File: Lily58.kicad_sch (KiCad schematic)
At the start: 40 parts, among them J1 USB_C_Receptacle, J2 USB_C_Receptacle, J3 Conn_01x03_Pin, U1 BQ24091DGQ, U2 TPS63000, U3 TPS63000, U4 ESP32-S3-WROOM-1, Y1 Crystal_GND24

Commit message: restructured schematic
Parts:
- removed U4: ESP32-S3-WROOM-1, PCM_Espressif:ESP32-S3-WROOM-1, symbol PCM_Espressif:ESP32-S3-WROOM-1
- removed Y1: Crystal_GND24, Crystal:Crystal_SMD_3225-4Pin_3.2x2.5mm_HandSoldering, symbol Device:Crystal_GND24
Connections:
- net +5V: no longer C11.1, J1.A4 (VBUS), J1.A9 (VBUS), J1.B4 (VBUS), J1.B9 (VBUS), J2.A4 (VBUS), J2.A9 (VBUS), J2.B4 (VBUS), J2.B9 (VBUS), U1.1 (IN)
- new net USB_5V: C11.1, J1.A4 (VBUS), J1.A9 (VBUS), J1.B4 (VBUS), J1.B9 (VBUS), J2.A4 (VBUS), J2.A9 (VBUS), J2.B4 (VBUS), J2.B9 (VBUS), U1.1 (IN)
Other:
- added sheet Microcontroller (microcontroller.kicad_sch)
- moved on the sheet: C1, C10, C11, C12, C2, C3, C4, C5, C6, C7, C8, C9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

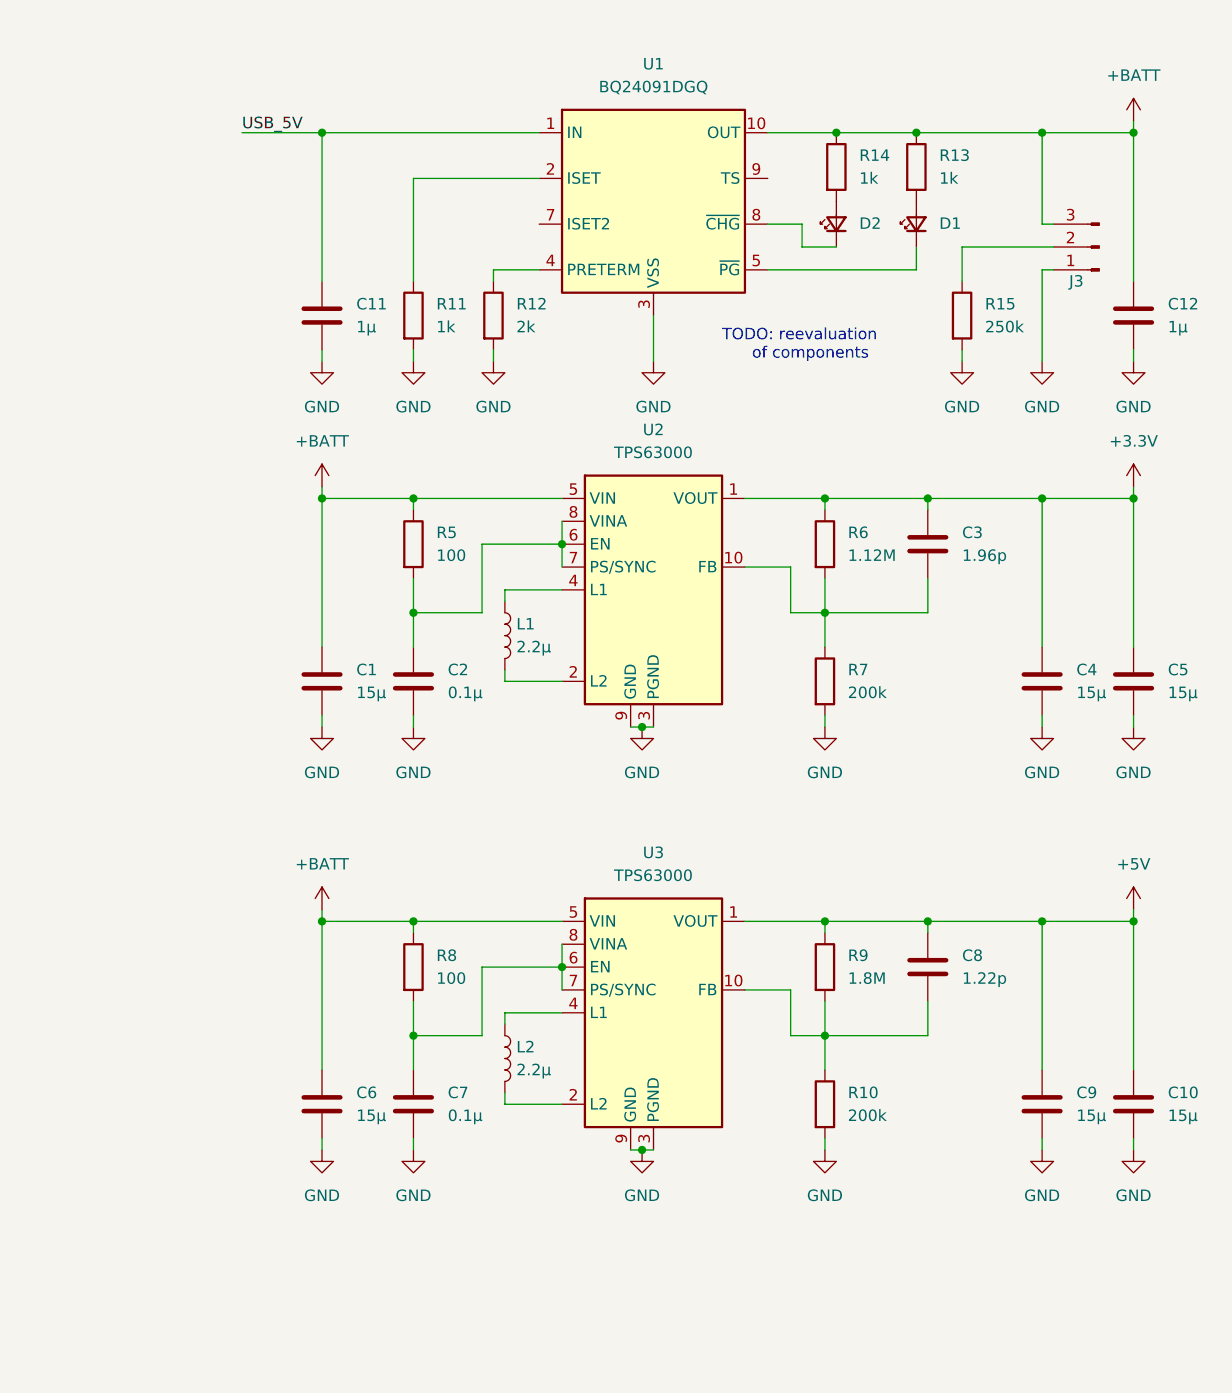
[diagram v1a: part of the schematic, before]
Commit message: configured battery charger circuit
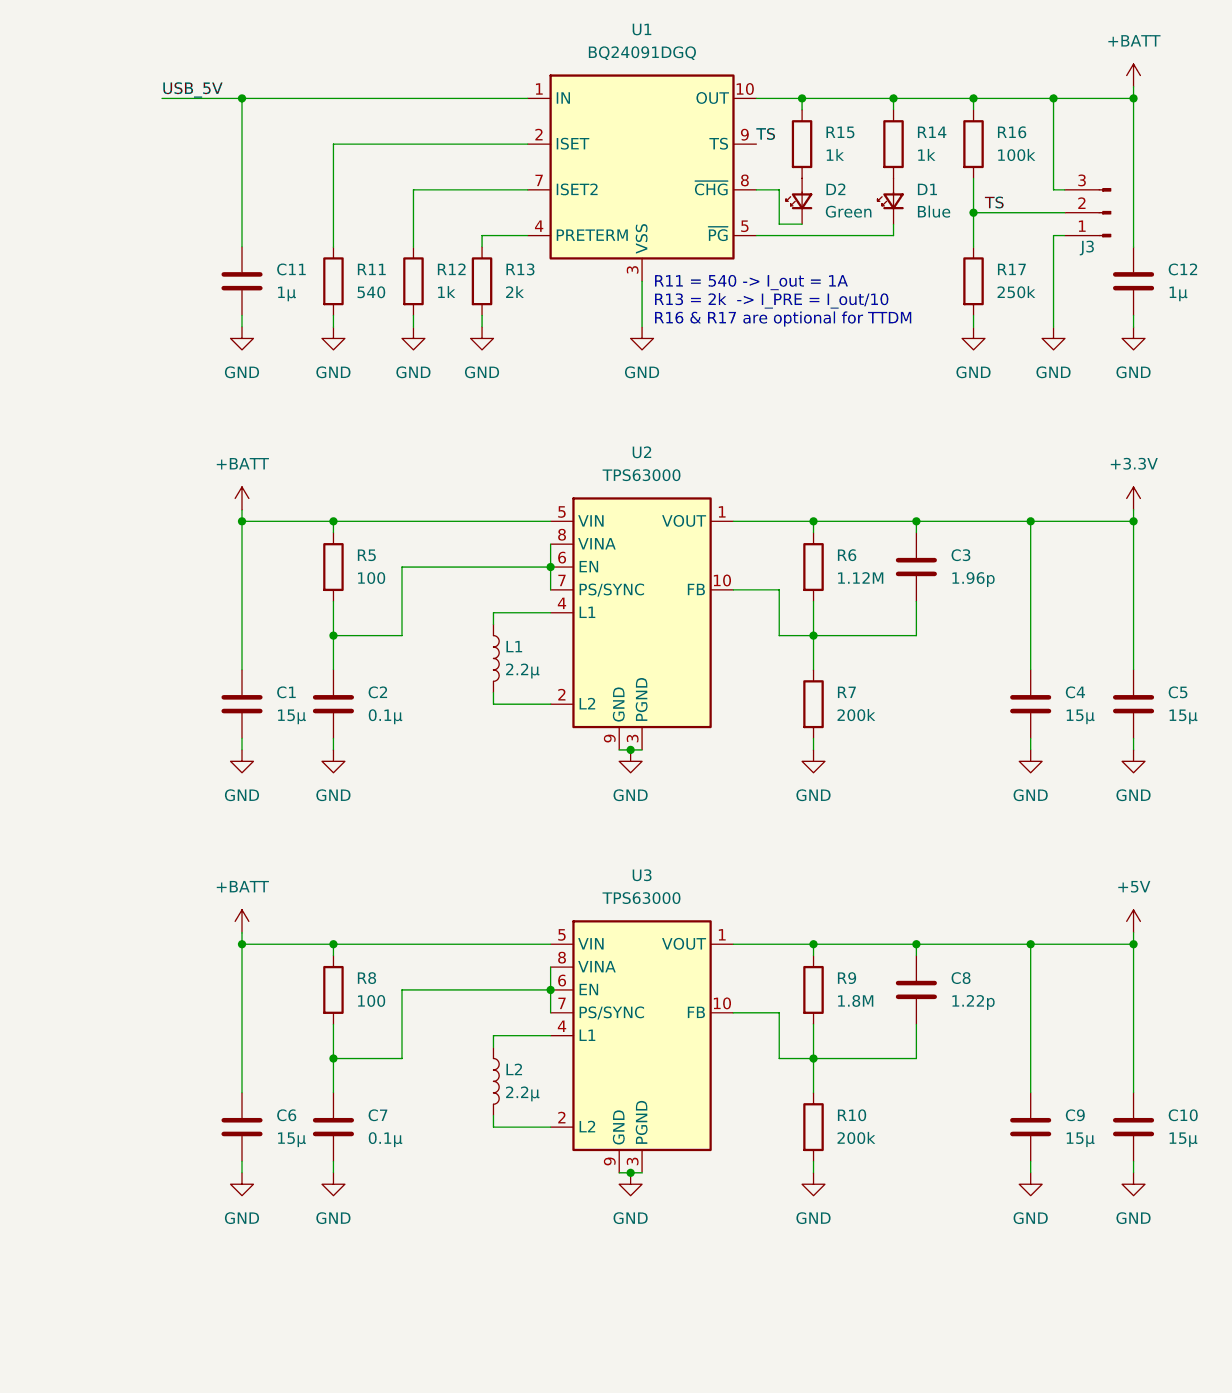
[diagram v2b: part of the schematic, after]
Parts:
- added R12: 1k, symbol Device:R
- added R16: 100k, symbol Device:R
- D1: value LED_Small -> Blue
- D2: value LED_Small -> Green
- R11: value 1k -> 540
- renumbered R12 to R13, R13 to R14, R14 to R15, R15 to R17
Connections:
- net +BATT: now also R16.1
- net GND: now also R12.2
- net TS: now reaches J3.2 (Pin_2), R17.1
- net TS: now also U1.9 (TS), R16.2
- net at U1.7 (ISET2): now also R12.1
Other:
- note added: "R11 = 540 -> I_out = 1A R13 = 2k -> I_PRE = I_out/10 R16 & R17 are optional for TTDM"
- note removed: "TODO: reevaluation of components"
- moved on the sheet: C1, C10, C11, C12, C2, C3, C4, C5, C6, C7, C8, C9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

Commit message: reworked component naming
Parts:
- renumbered C1 to C21, C2 to C22, C3 to C23, C4 to C24, C5 to C25, C6 to C31, C7 to C32, C8 to C33, C9 to C34, C10 to C35, L1 to L21, L2 to L31, R5 to R21, R6 to R22, R7 to R23, R8 to R31, R9 to R32, R10 to R33
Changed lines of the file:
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@@
   (symbol (lib_id "Device:C") (at 182.88 97.79 0) (unit 1)
     (in_bom yes) (on_board yes) (dnp no) (fields_autoplaced)
-    (property "Reference" "C2" (at 186.69 96.52 0)
+    (property "Reference" "C22" (at 186.69 96.52 0)
       (effects (font (size 1.27 1.27)) (justify left))
     )
@@
       (project "Lily58"
         (path "/a0958e12-2248-4ac3-b259-3086ac296b70"
-          (reference "C2") (unit 1)
+          (reference "C22") (unit 1)
         )
       )
@@
   (symbol (lib_id "Device:C") (at 271.78 97.79 0) (unit 1)
     (in_bom yes) (on_board yes) (dnp no) (fields_autoplaced)
-    (property "Reference" "C5" (at 275.59 96.52 0)
+    (property "Reference" "C25" (at 275.59 96.52 0)
       (effects (font (size 1.27 1.27)) (justify left))
     )
@@
       (project "Lily58"
         (path "/a0958e12-2248-4ac3-b259-3086ac296b70"
-          (reference "C5") (unit 1)
+          (reference "C25") (unit 1)
         )
       )
@@
   (symbol (lib_id "Device:L") (at 200.66 139.7 0) (unit 1)
     (in_bom yes) (on_board yes) (dnp no) (fields_autoplaced)
-    (property "Reference" "L2" (at 201.93 138.43 0)
+    (property "Reference" "L31" (at 201.93 138.43 0)
       (effects (font (size 1.27 1.27)) (justify left))
     )
@@
       (project "Lily58"
         (path "/a0958e12-2248-4ac3-b259-3086ac296b70"
-          (reference "L2") (unit 1)
+          (reference "L31") (unit 1)
         )
       )
@@
   (symbol (lib_id "Device:C") (at 247.65 129.54 0) (unit 1)
     (in_bom yes) (on_board yes) (dnp no) (fields_autoplaced)
-    (property "Reference" "C8" (at 251.46 128.27 0)
+    (property "Reference" "C33" (at 251.46 128.27 0)
       (effects (font (size 1.27 1.27)) (justify left))
     )
@@
       (project "Lily58"
         (path "/a0958e12-2248-4ac3-b259-3086ac296b70"
-          (reference "C8") (unit 1)
+          (reference "C33") (unit 1)
         )
       )
@@
   (symbol (lib_id "Device:C") (at 271.78 144.78 0) (unit 1)
     (in_bom yes) (on_board yes) (dnp no) (fields_autoplaced)
-    (property "Reference" "C10" (at 275.59 143.51 0)
+    (property "Reference" "C35" (at 275.59 143.51 0)
       (effects (font (size 1.27 1.27)) (justify left))
     )
@@
       (project "Lily58"
         (path "/a0958e12-2248-4ac3-b259-3086ac296b70"
-          (reference "C10") (unit 1)
+          (reference "C35") (unit 1)
         )
       )
@@
   (symbol (lib_id "Device:L") (at 200.66 92.71 0) (unit 1)
     (in_bom yes) (on_board yes) (dnp no) (fields_autoplaced)
-    (property "Reference" "L1" (at 201.93 91.44 0)
+    (property "Reference" "L21" (at 201.93 91.44 0)
       (effects (font (size 1.27 1.27)) (justify left))
     )
@@
       (project "Lily58"
         (path "/a0958e12-2248-4ac3-b259-3086ac296b70"
-          (reference "L1") (unit 1)
+          (reference "L21") (unit 1)
         )
       )
@@
   (symbol (lib_id "Device:C") (at 172.72 97.79 0) (unit 1)
     (in_bom yes) (on_board yes) (dnp no)
-    (property "Reference" "C1" (at 176.53 96.52 0)
+    (property "Reference" "C21" (at 176.53 96.52 0)
       (effects (font (size 1.27 1.27)) (justify left))
     )
@@
       (project "Lily58"
         (path "/a0958e12-2248-4ac3-b259-3086ac296b70"
-          (reference "C1") (unit 1)
+          (reference "C21") (unit 1)
         )
       )
@@
   (symbol (lib_id "Device:C") (at 172.72 144.78 0) (unit 1)
     (in_bom yes) (on_board yes) (dnp no)
-    (property "Reference" "C6" (at 176.53 143.51 0)
+    (property "Reference" "C31" (at 176.53 143.51 0)
       (effects (font (size 1.27 1.27)) (justify left))
     )
@@
       (project "Lily58"
         (path "/a0958e12-2248-4ac3-b259-3086ac296b70"
-          (reference "C6") (unit 1)
+          (reference "C31") (unit 1)
         )
       )
@@
   (symbol (lib_id "Device:C") (at 260.35 144.78 0) (unit 1)
     (in_bom yes) (on_board yes) (dnp no) (fields_autoplaced)
-    (property "Reference" "C9" (at 264.16 143.51 0)
+    (property "Reference" "C34" (at 264.16 143.51 0)
       (effects (font (size 1.27 1.27)) (justify left))
     )
@@
       (project "Lily58"
         (path "/a0958e12-2248-4ac3-b259-3086ac296b70"
-          (reference "C9") (unit 1)
+          (reference "C34") (unit 1)
         )
       )
@@
   (symbol (lib_id "Device:R") (at 236.22 97.79 0) (unit 1)
     (in_bom yes) (on_board yes) (dnp no) (fields_autoplaced)
-    (property "Reference" "R7" (at 238.76 96.52 0)
+    (property "Reference" "R23" (at 238.76 96.52 0)
       (effects (font (size 1.27 1.27)) (justify left))
     )
@@
       (project "Lily58"
         (path "/a0958e12-2248-4ac3-b259-3086ac296b70"
-          (reference "R7") (unit 1)
+          (reference "R23") (unit 1)
         )
       )
@@
   (symbol (lib_id "Device:C") (at 260.35 97.79 0) (unit 1)
     (in_bom yes) (on_board yes) (dnp no) (fields_autoplaced)
-    (property "Reference" "C4" (at 264.16 96.52 0)
+    (property "Reference" "C24" (at 264.16 96.52 0)
       (effects (font (size 1.27 1.27)) (justify left))
     )
@@
       (project "Lily58"
         (path "/a0958e12-2248-4ac3-b259-3086ac296b70"
-          (reference "C4") (unit 1)
+          (reference "C24") (unit 1)
         )
       )
@@
   (symbol (lib_id "Device:R") (at 236.22 129.54 0) (unit 1)
     (in_bom yes) (on_board yes) (dnp no) (fields_autoplaced)
-    (property "Reference" "R9" (at 238.76 128.27 0)
+    (property "Reference" "R32" (at 238.76 128.27 0)
       (effects (font (size 1.27 1.27)) (justify left))
     )
@@
       (project "Lily58"
         (path "/a0958e12-2248-4ac3-b259-3086ac296b70"
-          (reference "R9") (unit 1)
+          (reference "R32") (unit 1)
         )
       )
@@
   (symbol (lib_id "Device:R") (at 236.22 82.55 0) (unit 1)
     (in_bom yes) (on_board yes) (dnp no) (fields_autoplaced)
-    (property "Reference" "R6" (at 238.76 81.28 0)
+    (property "Reference" "R22" (at 238.76 81.28 0)
       (effects (font (size 1.27 1.27)) (justify left))
     )
@@
       (project "Lily58"
         (path "/a0958e12-2248-4ac3-b259-3086ac296b70"
-          (reference "R6") (unit 1)
+          (reference "R22") (unit 1)
         )
       )
@@
   (symbol (lib_id "Device:R") (at 182.88 129.54 0) (unit 1)
     (in_bom yes) (on_board yes) (dnp no) (fields_autoplaced)
-    (property "Reference" "R8" (at 185.42 128.27 0)
+    (property "Reference" "R31" (at 185.42 128.27 0)
       (effects (font (size 1.27 1.27)) (justify left))
     )
@@
       (project "Lily58"
         (path "/a0958e12-2248-4ac3-b259-3086ac296b70"
-          (reference "R8") (unit 1)
+          (reference "R31") (unit 1)
         )
       )
@@
   (symbol (lib_id "Device:C") (at 182.88 144.78 0) (unit 1)
     (in_bom yes) (on_board yes) (dnp no) (fields_autoplaced)
-    (property "Reference" "C7" (at 186.69 143.51 0)
+    (property "Reference" "C32" (at 186.69 143.51 0)
       (effects (font (size 1.27 1.27)) (justify left))
     )
@@
       (project "Lily58"
         (path "/a0958e12-2248-4ac3-b259-3086ac296b70"
-          (reference "C7") (unit 1)
+          (reference "C32") (unit 1)
         )
       )
@@
   (symbol (lib_id "Device:R") (at 182.88 82.55 0) (unit 1)
     (in_bom yes) (on_board yes) (dnp no) (fields_autoplaced)
-    (property "Reference" "R5" (at 185.42 81.28 0)
+    (property "Reference" "R21" (at 185.42 81.28 0)
       (effects (font (size 1.27 1.27)) (justify left))
     )
@@
       (project "Lily58"
         (path "/a0958e12-2248-4ac3-b259-3086ac296b70"
-          (reference "R5") (unit 1)
+          (reference "R21") (unit 1)
         )
       )
@@
   (symbol (lib_id "Device:C") (at 247.65 82.55 0) (unit 1)
     (in_bom yes) (on_board yes) (dnp no) (fields_autoplaced)
-    (property "Reference" "C3" (at 251.46 81.28 0)
+    (property "Reference" "C23" (at 251.46 81.28 0)
       (effects (font (size 1.27 1.27)) (justify left))
     )
@@
       (project "Lily58"
         (path "/a0958e12-2248-4ac3-b259-3086ac296b70"
-          (reference "C3") (unit 1)
+          (reference "C23") (unit 1)
         )
       )
@@
   (symbol (lib_id "Device:R") (at 236.22 144.78 0) (unit 1)
     (in_bom yes) (on_board yes) (dnp no) (fields_autoplaced)
-    (property "Reference" "R10" (at 238.76 143.51 0)
+    (property "Reference" "R33" (at 238.76 143.51 0)
       (effects (font (size 1.27 1.27)) (justify left))
     )
@@
       (project "Lily58"
         (path "/a0958e12-2248-4ac3-b259-3086ac296b70"
-          (reference "R10") (unit 1)
-        )
-      )
+          (reference "R33") (unit 1)
+        )
+      )

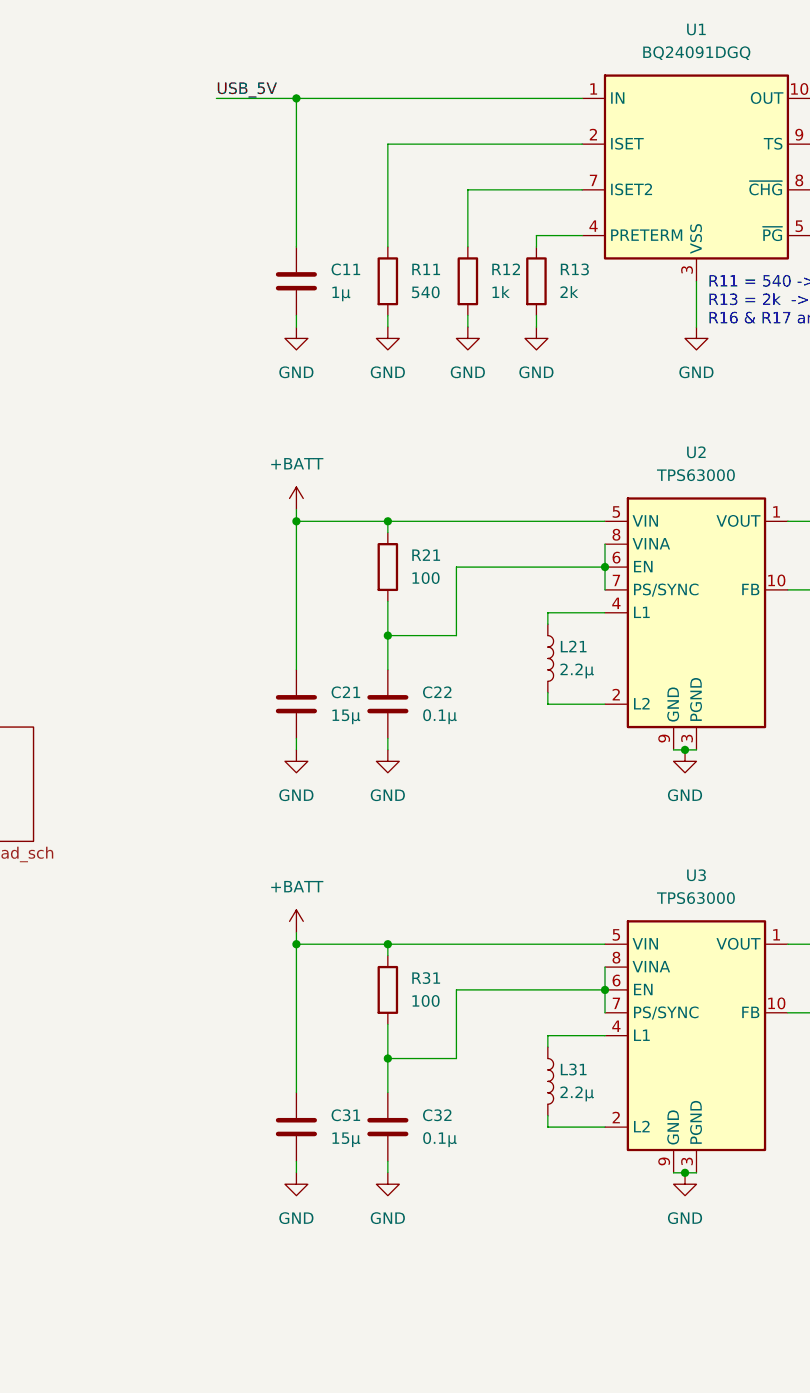
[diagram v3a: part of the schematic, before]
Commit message: added ESP32 circuitry
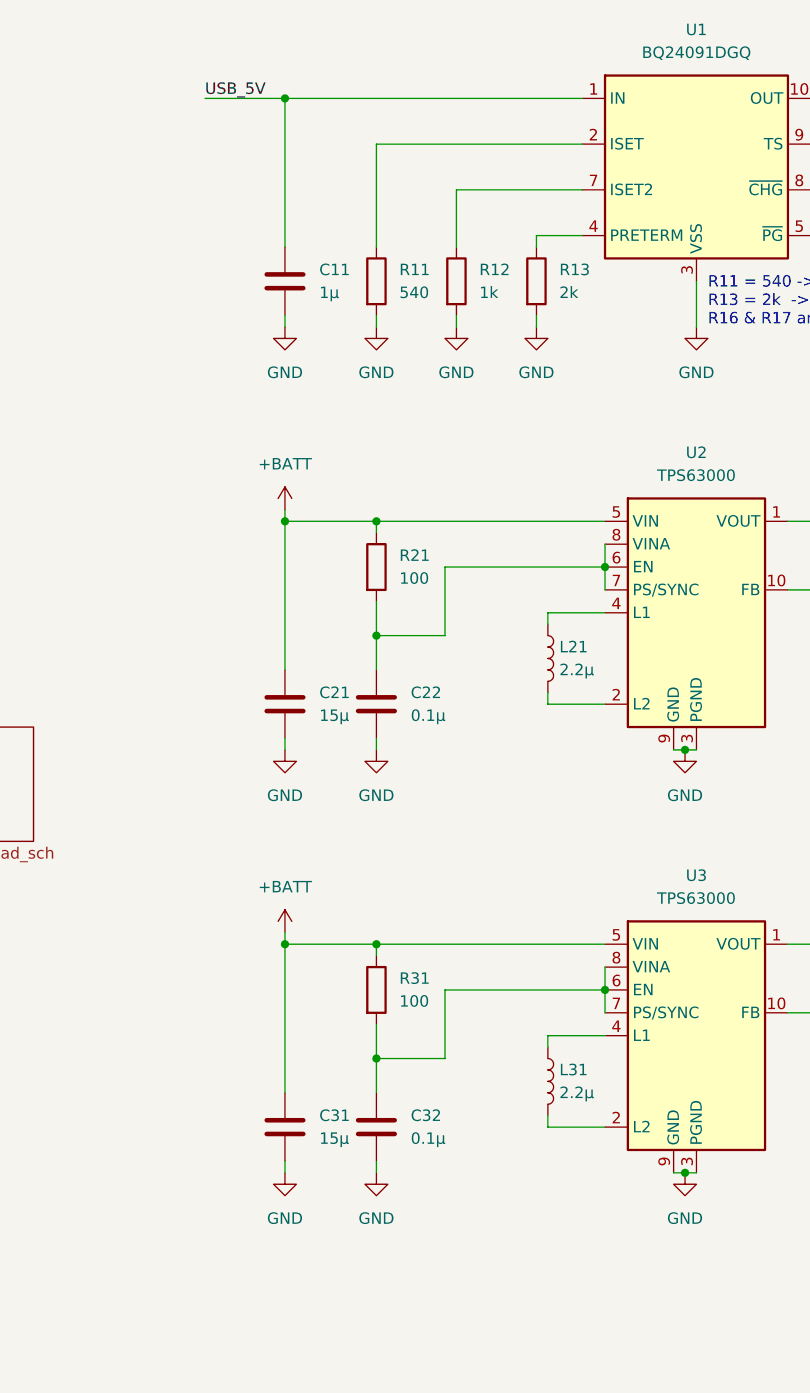
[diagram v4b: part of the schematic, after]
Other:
- moved on the sheet: C11, C21, C22, C31, C32, R11, R12, R21, R31
